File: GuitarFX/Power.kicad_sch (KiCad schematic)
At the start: 20 parts, among them J1 Jack-DC, U3 NCP718xSN500, U4 NCP1117-3.3_SOT223

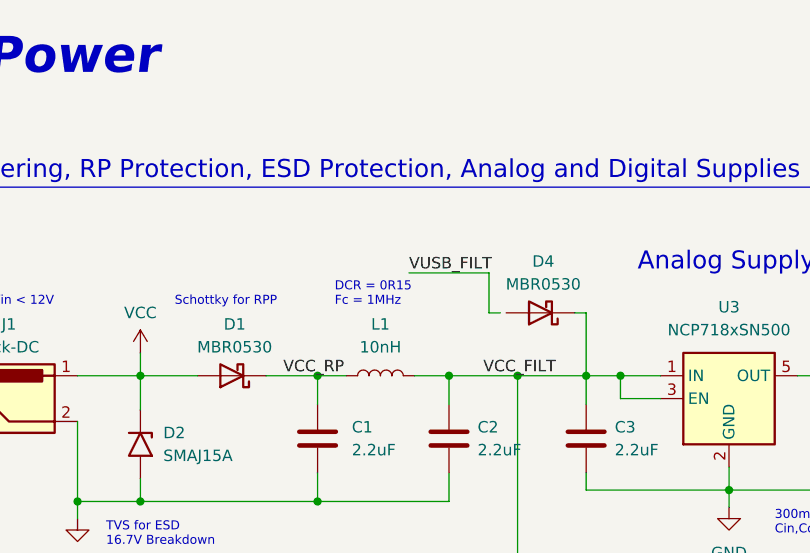
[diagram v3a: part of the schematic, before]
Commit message: Added decuopling capacitors and filtering to MCU
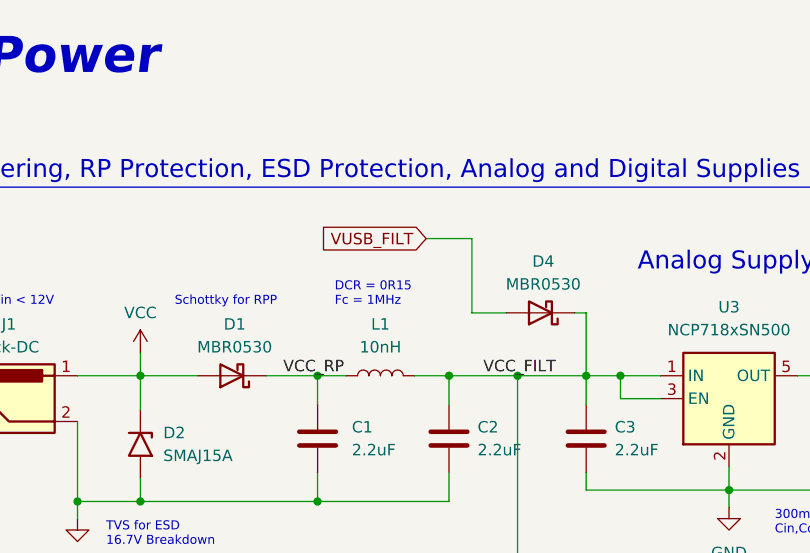
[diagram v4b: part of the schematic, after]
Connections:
- net VUSB_FILT: now also D4.2 (A)
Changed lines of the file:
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@@
     (stroke (width 0) (type default))
   )
-  (wire (pts (xy 107.95 55.88) (xy 106.68 55.88))
+  (wire (pts (xy 104.775 55.88) (xy 108.585 55.88))
     (stroke (width 0) (type default))
   )
@@
     (stroke (width 0) (type default))
   )
-  (wire (pts (xy 97.79 51.435) (xy 106.68 51.435))
+  (wire (pts (xy 99.695 47.625) (xy 104.775 47.625))
     (stroke (width 0) (type default))
   )
@@
     (stroke (width 0) (type default))
   )
-  (wire (pts (xy 106.68 55.88) (xy 106.68 51.435))
+  (wire (pts (xy 104.775 55.88) (xy 104.775 47.625))
     (stroke (width 0) (type default))
   )
@@
     (effects (font (size 1.27 1.27)) (justify left bottom))
   )
-  (label "VUSB_FILT" (at 97.79 51.435 0) (fields_autoplaced)
-    (effects (font (size 1.27 1.27)) (justify left bottom))
-  )
   (label "VCC_FILT" (at 106.045 62.865 0) (fields_autoplaced)
     (effects (font (size 1.27 1.27)) (justify left bottom))
@@
     (effects (font (size 1.27 1.27)) (justify left bottom))
   )
+  (global_label "VUSB_FILT" (shape input) (at 99.695 47.625 180) (fields_autoplaced)
+    (effects (font (size 1.27 1.27)) (justify right))
+    (property "Intersheetrefs" "${INTERSHEET_REFS}" (at 87.1545 47.625 0)
+      (effects (font (size 1.27 1.27)) (justify right) hide)
+    )
+  )
   (symbol (lib_id "power:GND") (at 172.085 115.57 0) (unit 1)

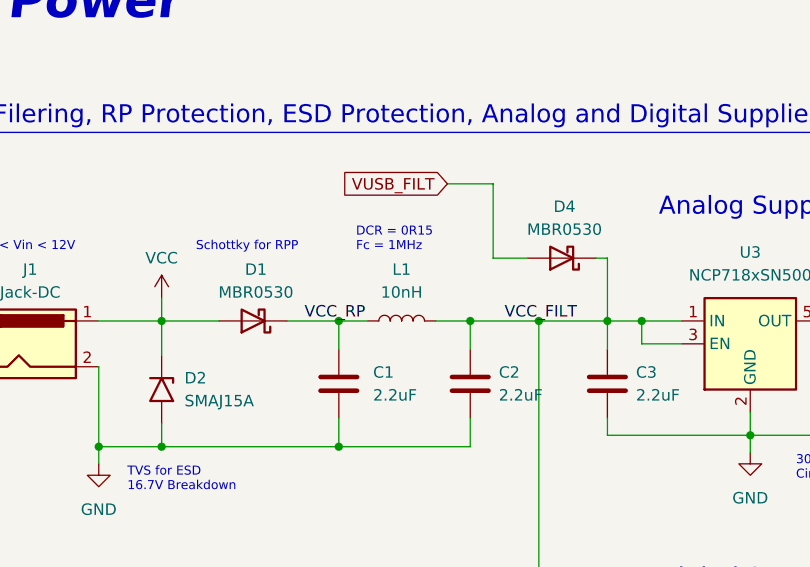
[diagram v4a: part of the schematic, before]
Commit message: Added USB-C connector to schematic and changed inductors in filters to ferrites
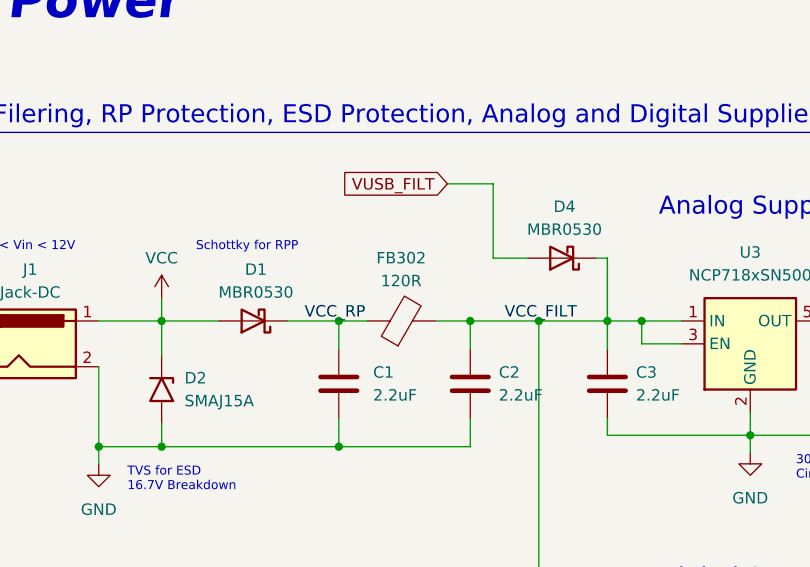
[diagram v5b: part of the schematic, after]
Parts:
- removed L1: 10nH, symbol Device:L
- added FB302: 120R, symbol Device:FerriteBead
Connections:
- net VCC_FILT: now also FB302.2
- net VCC_RP: now also FB302.1
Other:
- note removed: "DCR = 0R15 Fc = 1MHz"
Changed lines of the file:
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@@
-    (effects (font (size 1 1)) (justify left bottom))
-  )
-  (text "DCR = 0R15\nFc = 1MHz" (at 89.535 55.245 0)
     (effects (font (size 1 1)) (justify left bottom))
   )
@@
     )
   )
-  (symbol (lib_id "Device:L") (at 94.615 62.865 90) (unit 1)
-    (in_bom yes) (on_board yes) (dnp no) (fields_autoplaced)
-    (property "Reference" "L1" (at 94.615 57.15 90)
-      (effects (font (size 1.27 1.27)))
-    )
-    (property "Value" "10nH" (at 94.615 59.69 90)
-      (effects (font (size 1.27 1.27)))
-    )
-    (property "Footprint" "" (at 94.615 62.865 0)
-      (effects (font (size 1.27 1.27)) hide)
-    )
-    (property "Datasheet" "~" (at 94.615 62.865 0)
-      (effects (font (size 1.27 1.27)) hide)
-    )
-    (pin "1")
-    (pin "2")
-    (instances
-      (project "GuitarFX"
-        (path "/4ab4bfc6-98ca-4cb1-8273-436b96035b51/171d6b95-1f9c-4c9d-954a-bc461d0cb77a"
-          (reference "L1") (unit 1)
-        )
-      )
-    )
-  )
   (symbol (lib_id "Device:R") (at 162.56 62.865 90) (unit 1)
     (in_bom yes) (on_board yes) (dnp no) (fields_autoplaced)
@@
         )
       )
+    )
+  )
+  (symbol (lib_id "Device:FerriteBead") (at 94.615 62.865 90) (unit 1)
+    (in_bom yes) (on_board yes) (dnp no)
+    (property "Reference" "FB302" (at 94.5642 55.88 90)
+      (effects (font (size 1.27 1.27)))
+    )
+    (property "Value" "120R" (at 94.5642 58.42 90)
+      (effects (font (size 1.27 1.27)))
+    )
+    (property "Footprint" "" (at 94.615 64.643 90)
+      (effects (font (size 1.27 1.27)) hide)
+    )
+    (property "Datasheet" "~" (at 94.615 62.865 0)
+      (effects (font (size 1.27 1.27)) hide)
+    )
+    (pin "1")
+    (pin "2")
+    (instances
+      (project "GuitarFX"
+        (path "/4ab4bfc6-98ca-4cb1-8273-436b96035b51/cf97d527-62da-4324-8e3d-11052c92c164"
+          (reference "FB302") (unit 1)
+        )
+        (path "/4ab4bfc6-98ca-4cb1-8273-436b96035b51/171d6b95-1f9c-4c9d-954a-bc461d0cb77a"
+          (reference "FB201") (unit 1)
+        )
+      )

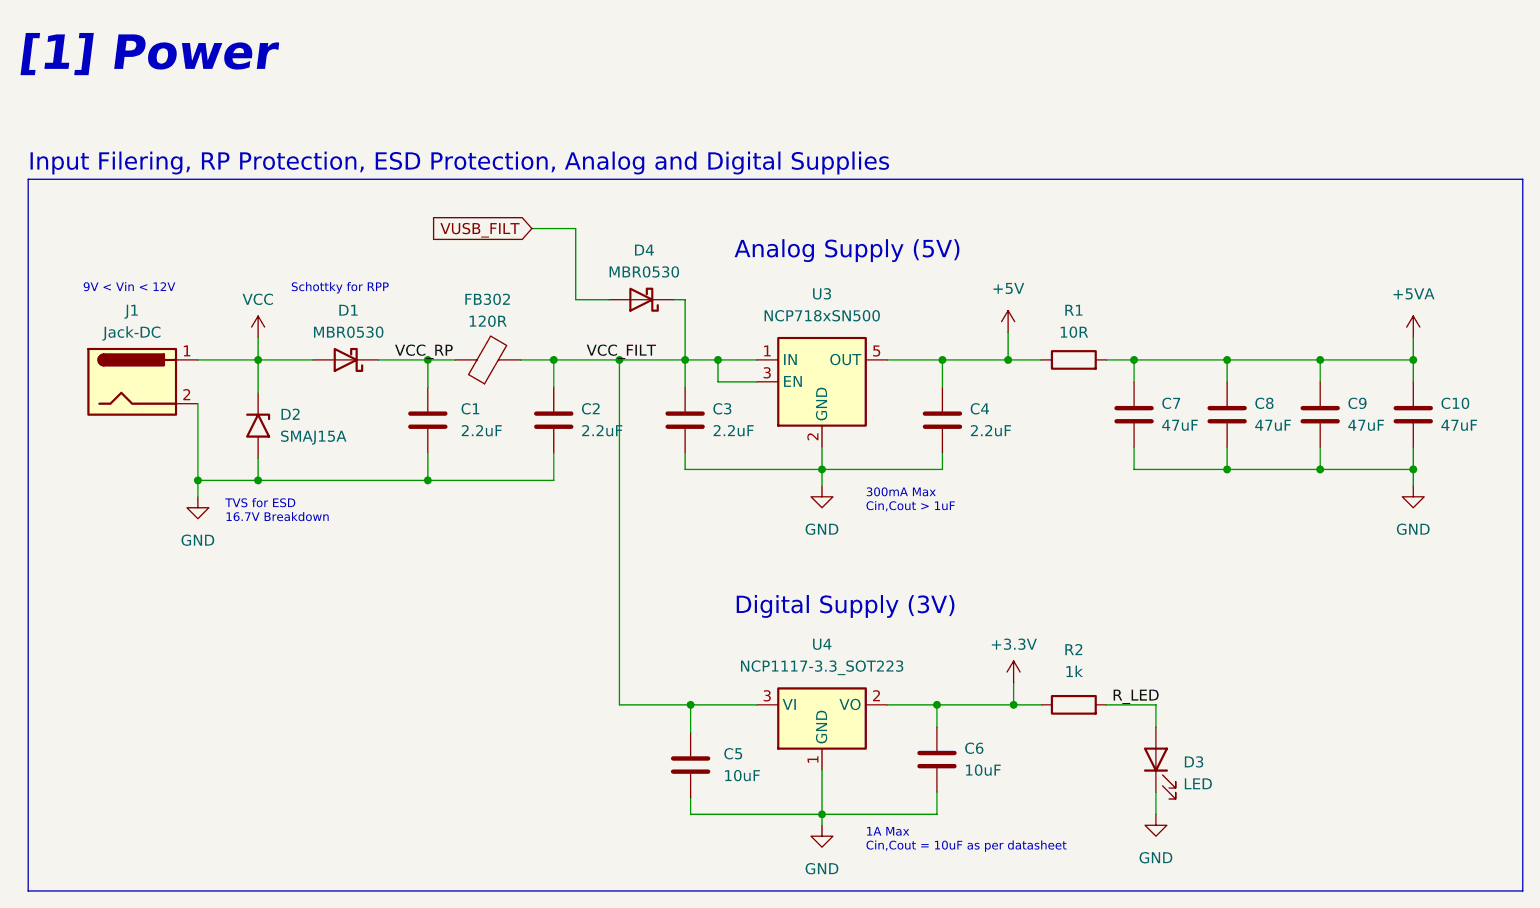
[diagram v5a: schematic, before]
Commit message: Added RGB LEDs and ADC connections for potentiometer readings along with connector
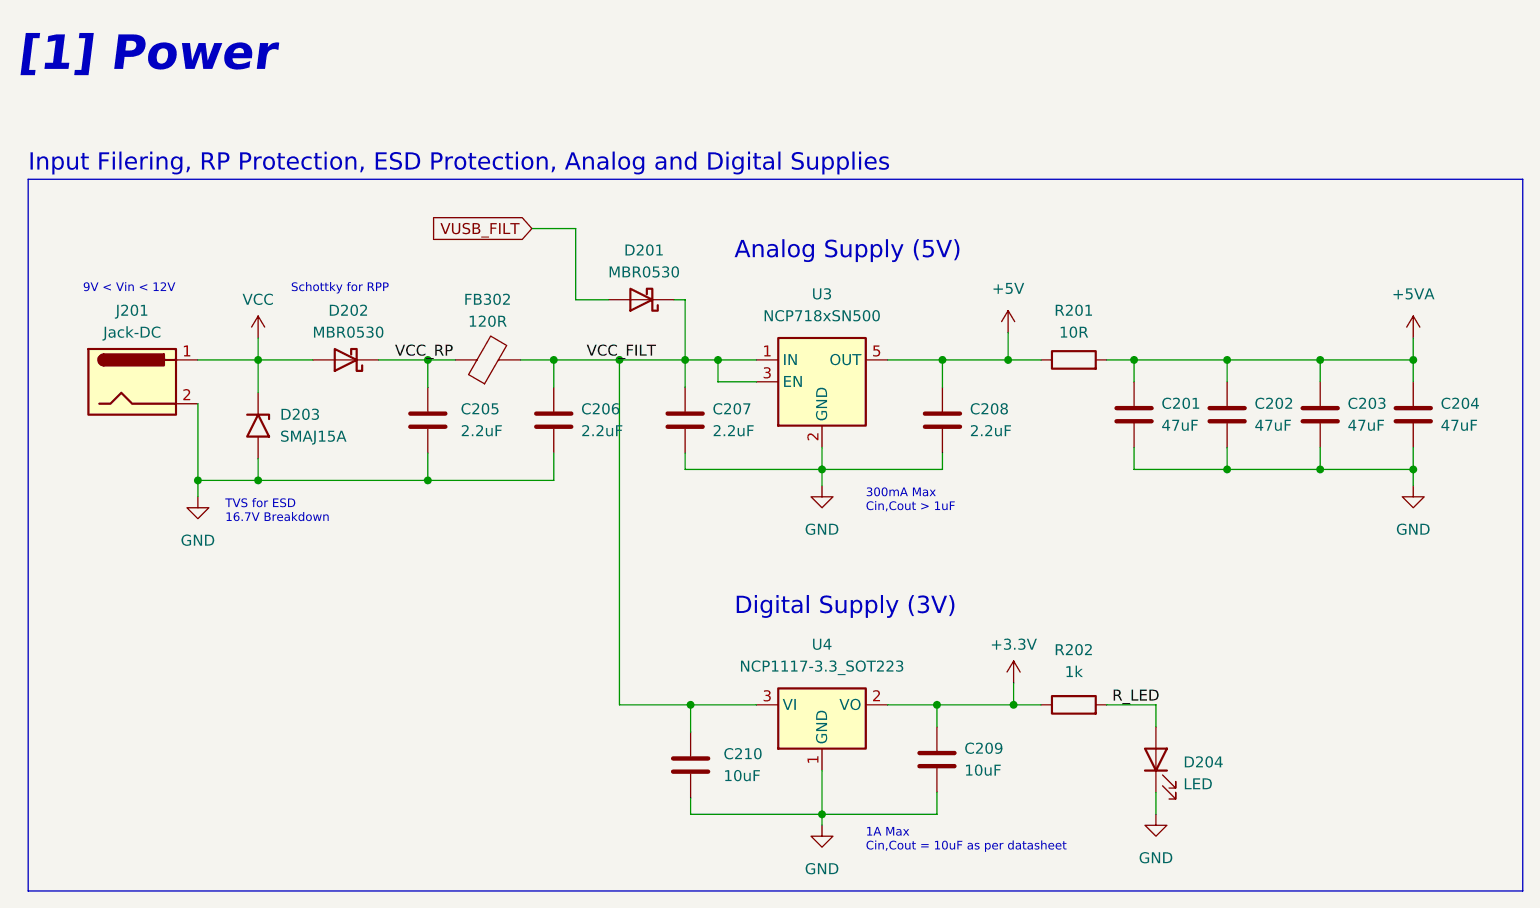
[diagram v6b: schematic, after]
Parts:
- renumbered C7 to C201, C8 to C202, C9 to C203, C10 to C204, C1 to C205, C2 to C206, C3 to C207, C4 to C208, C6 to C209, C5 to C210, D4 to D201, D1 to D202, D2 to D203, D3 to D204, J1 to J201, R1 to R201, R2 to R202

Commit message: Got rid of most ERC violations
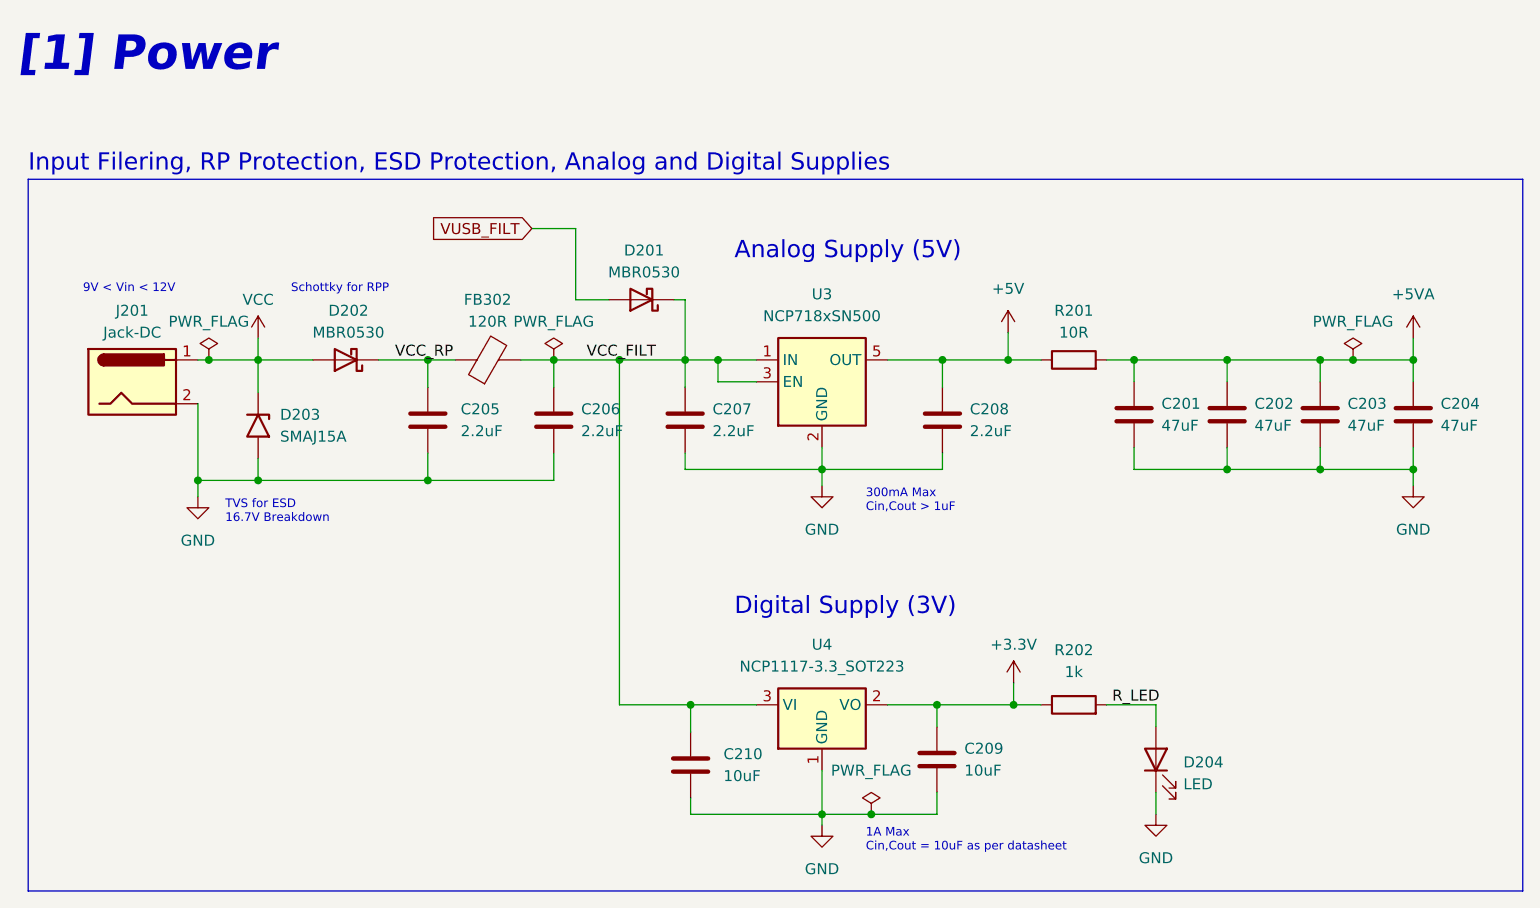
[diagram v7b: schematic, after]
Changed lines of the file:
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@@
   (junction (at 155.575 102.87) (diameter 0) (color 0 0 0 0)
   )
+  (junction (at 62.23 62.865) (diameter 0) (color 0 0 0 0)
+  )
   (junction (at 87.63 76.835) (diameter 0) (color 0 0 0 0)
   )
   (junction (at 191.135 62.865) (diameter 0) (color 0 0 0 0)
   )
+  (junction (at 139.065 115.57) (diameter 0) (color 0 0 0 0)
+  )
   (junction (at 118.11 102.87) (diameter 0) (color 0 0 0 0)
   )
   (junction (at 121.285 62.865) (diameter 0) (color 0 0 0 0)
   )
+  (junction (at 194.945 62.865) (diameter 0) (color 0 0 0 0)
+  )
   (junction (at 180.34 75.565) (diameter 0) (color 0 0 0 0)
   )
@@
     (stroke (width 0) (type default))
   )
+  (wire (pts (xy 139.065 115.57) (xy 133.35 115.57))
+    (stroke (width 0) (type default))
+  )
   (wire (pts (xy 81.915 62.865) (xy 87.63 62.865))
     (stroke (width 0) (type default))
@@
     (stroke (width 0) (type default))
   )
-  (wire (pts (xy 60.96 62.865) (xy 67.945 62.865))
+  (wire (pts (xy 60.96 62.865) (xy 62.23 62.865))
     (stroke (width 0) (type default))
   )
@@
     (stroke (width 0) (type default))
   )
+  (wire (pts (xy 194.945 62.865) (xy 201.93 62.865))
+    (stroke (width 0) (type default))
+  )
   (wire (pts (xy 102.235 62.865) (xy 102.235 66.04))
     (stroke (width 0) (type default))
   )
-  (wire (pts (xy 146.685 115.57) (xy 133.35 115.57))
+  (wire (pts (xy 62.23 62.865) (xy 67.945 62.865))
     (stroke (width 0) (type default))
   )
@@
     (stroke (width 0) (type default))
   )
-  (wire (pts (xy 191.135 62.865) (xy 201.93 62.865))
+  (wire (pts (xy 191.135 62.865) (xy 194.945 62.865))
     (stroke (width 0) (type default))
   )
@@
   )
   (wire (pts (xy 98.425 62.865) (xy 102.235 62.865))
+    (stroke (width 0) (type default))
+  )
+  (wire (pts (xy 139.065 115.57) (xy 146.685 115.57))
     (stroke (width 0) (type default))
   )
@@
     )
   )
+  (symbol (lib_id "power:PWR_FLAG") (at 194.945 62.865 0) (unit 1)
+    (in_bom yes) (on_board yes) (dnp no) (fields_autoplaced)
+    (property "Reference" "#FLG0202" (at 194.945 60.96 0)
+      (effects (font (size 1.27 1.27)) hide)
+    )
+    (property "Value" "PWR_FLAG" (at 194.945 58.42 0)
+      (effects (font (size 1.27 1.27)))
+    )
+    (property "Footprint" "" (at 194.945 62.865 0)
+      (effects (font (size 1.27 1.27)) hide)
+    )
+    (property "Datasheet" "~" (at 194.945 62.865 0)
+      (effects (font (size 1.27 1.27)) hide)
+    )
+    (pin "1")
+    (instances
+      (project "GuitarFX"
+        (path "/4ab4bfc6-98ca-4cb1-8273-436b96035b51/171d6b95-1f9c-4c9d-954a-bc461d0cb77a"
+          (reference "#FLG0202") (unit 1)
+        )
+      )
+    )
+  )
   (symbol (lib_id "power:GND") (at 201.93 77.47 0) (unit 1)
     (in_bom yes) (on_board yes) (dnp no) (fields_autoplaced)
@@
     )
   )
+  (symbol (lib_id "power:PWR_FLAG") (at 62.23 62.865 0) (unit 1)
+    (in_bom yes) (on_board yes) (dnp no) (fields_autoplaced)
+    (property "Reference" "#FLG0201" (at 62.23 60.96 0)
+      (effects (font (size 1.27 1.27)) hide)
+    )
+    (property "Value" "PWR_FLAG" (at 62.23 58.42 0)
+      (effects (font (size 1.27 1.27)))
+    )
+    (property "Footprint" "" (at 62.23 62.865 0)
+      (effects (font (size 1.27 1.27)) hide)
+    )
+    (property "Datasheet" "~" (at 62.23 62.865 0)
+      (effects (font (size 1.27 1.27)) hide)
+    )
+    (pin "1")
+    (instances
+      (project "GuitarFX"
+        (path "/4ab4bfc6-98ca-4cb1-8273-436b96035b51/171d6b95-1f9c-4c9d-954a-bc461d0cb77a"
+          (reference "#FLG0201") (unit 1)
+        )
+      )
+    )
+  )
   (symbol (lib_id "Device:C") (at 147.32 69.85 0) (unit 1)
     (in_bom yes) (on_board yes) (dnp no) (fields_autoplaced)
@@
         (path "/4ab4bfc6-98ca-4cb1-8273-436b96035b51/171d6b95-1f9c-4c9d-954a-bc461d0cb77a"
           (reference "C206") (unit 1)
+        )
+      )
+    )
+  )
+  (symbol (lib_id "power:PWR_FLAG") (at 139.065 115.57 0) (unit 1)
+    (in_bom yes) (on_board yes) (dnp no) (fields_autoplaced)
+    (property "Reference" "#FLG0204" (at 139.065 113.665 0)
+      (effects (font (size 1.27 1.27)) hide)
+    )
+    (property "Value" "PWR_FLAG" (at 139.065 110.49 0)
+      (effects (font (size 1.27 1.27)))
+    )
+    (property "Footprint" "" (at 139.065 115.57 0)
+      (effects (font (size 1.27 1.27)) hide)
+    )
+    (property "Datasheet" "~" (at 139.065 115.57 0)
+      (effects (font (size 1.27 1.27)) hide)
+    )
+    (pin "1")
+    (instances
+      (project "GuitarFX"
+        (path "/4ab4bfc6-98ca-4cb1-8273-436b96035b51/171d6b95-1f9c-4c9d-954a-bc461d0cb77a"
+          (reference "#FLG0204") (unit 1)
         )
       )
@@
         )
       )
+    )
+  )
+  (symbol (lib_id "power:PWR_FLAG") (at 102.235 62.865 0) (unit 1)
+    (in_bom yes) (on_board yes) (dnp no) (fields_autoplaced)
+    (property "Reference" "#FLG0203" (at 102.235 60.96 0)
+      (effects (font (size 1.27 1.27)) hide)
+    )
+    (property "Value" "PWR_FLAG" (at 102.235 58.42 0)
+      (effects (font (size 1.27 1.27)))
+    )
+    (property "Footprint" "" (at 102.235 62.865 0)
+      (effects (font (size 1.27 1.27)) hide)
+    )
+    (property "Datasheet" "~" (at 102.235 62.865 0)
+      (effects (font (size 1.27 1.27)) hide)
+    )
+    (pin "1")
+    (instances
+      (project "GuitarFX"
+        (path "/4ab4bfc6-98ca-4cb1-8273-436b96035b51/171d6b95-1f9c-4c9d-954a-bc461d0cb77a"
+          (reference "#FLG0203") (unit 1)
+        )
+      )
